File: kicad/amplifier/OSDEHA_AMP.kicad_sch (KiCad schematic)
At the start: 59 parts, among them J1 INPUT, J2 HEATERS DC, J3 PSU HV, J4 OUTPUT, J5 DHT FIL, Q1 DN2540, Q2 DN2540, Q3 STF3LN80K5, Q4 STF3LN80K5, SW1 SW_DPDT_x2, U1 6E5P, U2 6E5P, U3 801A, U4 801A

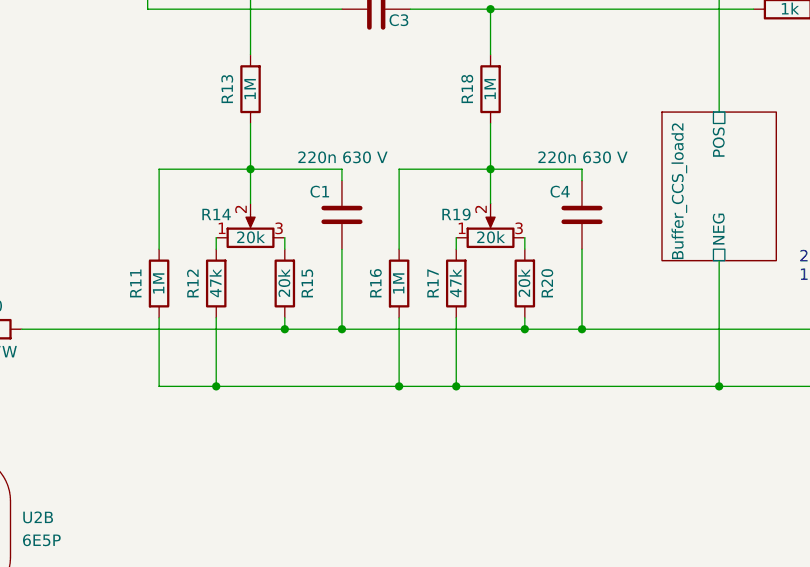
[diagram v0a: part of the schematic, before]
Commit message: adjust values of R15 and R20 by measurement of Vbias
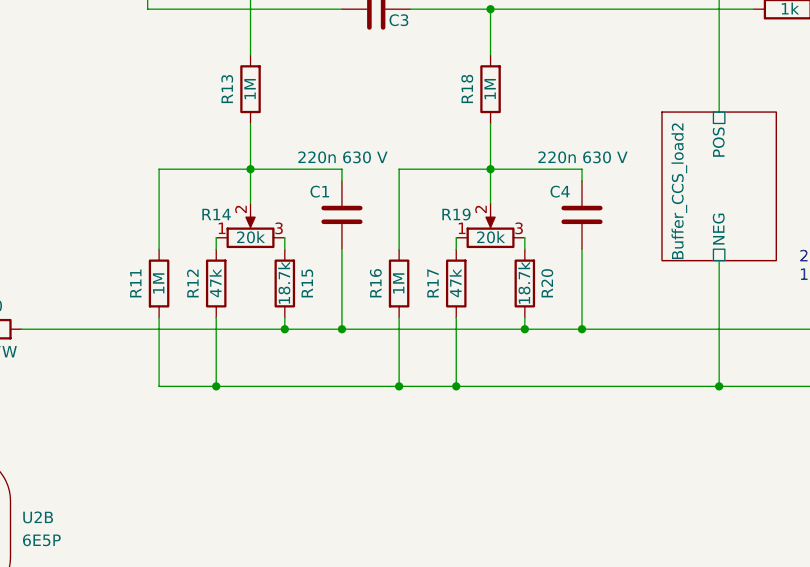
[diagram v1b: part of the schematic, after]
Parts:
- R15, R20: value 20k -> 18.7k
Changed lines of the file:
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@@
 			)
 		)
-		(property "Value" "20k"
+		(property "Value" "18.7k"
 			(at 191.77 173.99 90)
 			(effects
@@
 			)
 		)
-		(property "Value" "20k"
+		(property "Value" "18.7k"
 			(at 165.1 173.99 90)
 			(effects

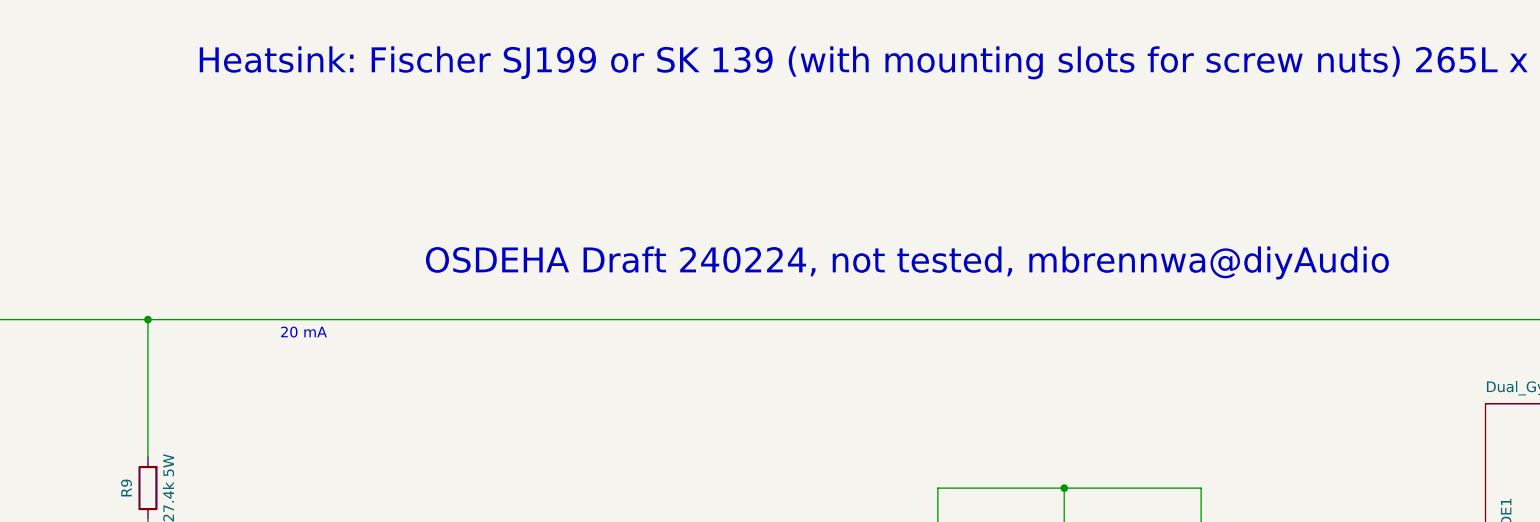
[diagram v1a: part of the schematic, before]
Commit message: draft date on schematic
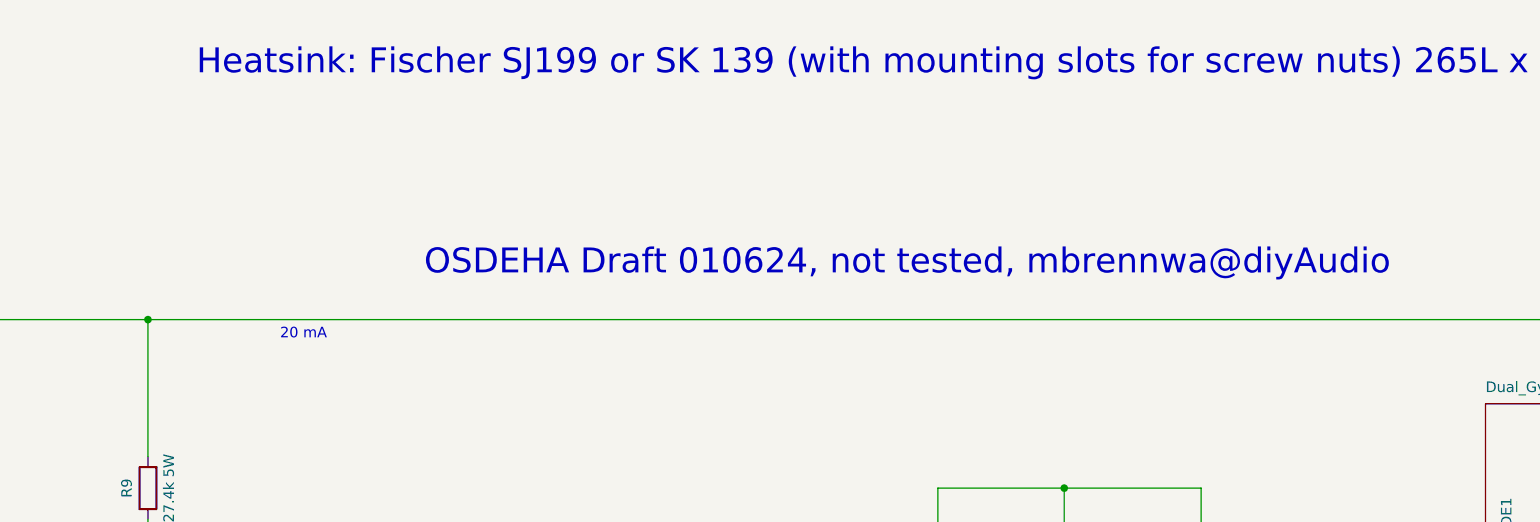
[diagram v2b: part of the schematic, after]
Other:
- note added: "OSDEHA Draft 010624, not tested, mbrennwa@diyAudio"
- note removed: "OSDEHA Draft 240224, not tested, mbrennwa@diyAudio"
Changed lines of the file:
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@@
 		)
 	)
-	(text "OSDEHA Draft 240224, not tested, mbrennwa@diyAudio"
+	(text "OSDEHA Draft 010624, not tested, mbrennwa@diyAudio"
 		(exclude_from_sim no)
 		(at 279.4 69.85 0)

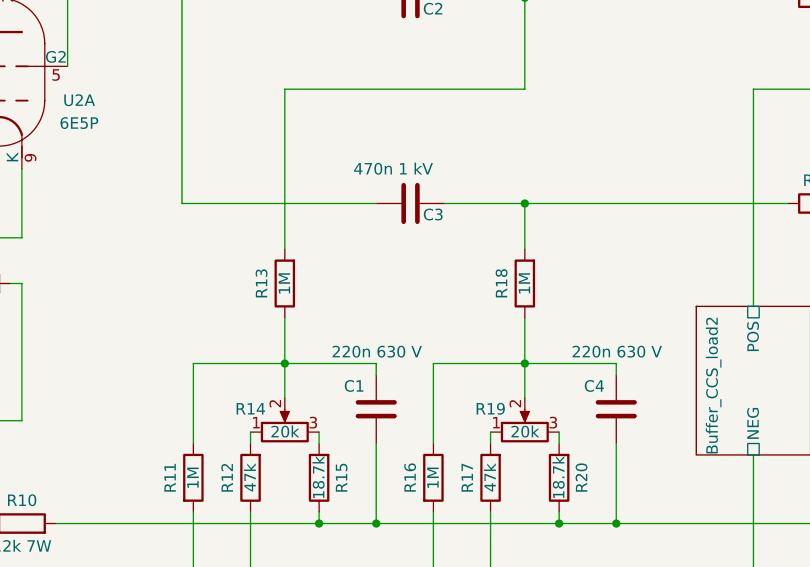
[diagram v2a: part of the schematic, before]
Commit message: changed R13 and R18 from 1M to 100k in schematic and PCB
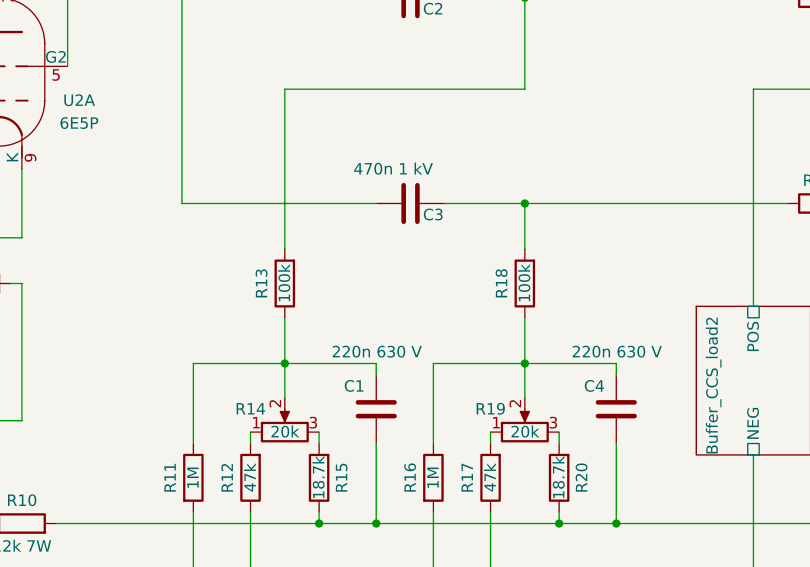
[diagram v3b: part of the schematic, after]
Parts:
- R13, R18: value 1M -> 100k
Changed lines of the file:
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@@
 			)
 		)
-		(property "Value" "1M"
+		(property "Value" "100k"
 			(at 161.29 152.4 90)
 			(effects
@@
 			)
 		)
-		(property "Value" "1M"
+		(property "Value" "100k"
 			(at 187.96 152.4 90)
 			(effects

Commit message: revise R values in schematic and PCB files. Expand test/design notes.
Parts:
- R13: MPN CMF551M0000 -> CMF55100K00
- R18: MPN CMF551M000 -> CMF55100K00
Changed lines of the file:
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@@
 			)
 		)
-		(property "MPN" "CMF551M0000"
+		(property "MPN" "CMF55100K00"
 			(at 161.29 152.4 90)
 			(effects
@@
 			)
 		)
-		(property "MPN" "CMF551M000"
+		(property "MPN" "CMF55100K00"
 			(at 187.96 152.4 90)
 			(effects

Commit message: cleanup
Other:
- note added: "OSDEHA Draft DDMMYY, not tested, mbrennwa@diyAudio"
- note removed: "OSDEHA Draft 010624, not tested, mbrennwa@diyAudio"
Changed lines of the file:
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@@
 		)
 	)
-	(text "OSDEHA Draft 010624, not tested, mbrennwa@diyAudio"
+	(text "OSDEHA Draft DDMMYY, not tested, mbrennwa@diyAudio"
 		(exclude_from_sim no)
 		(at 279.4 69.85 0)

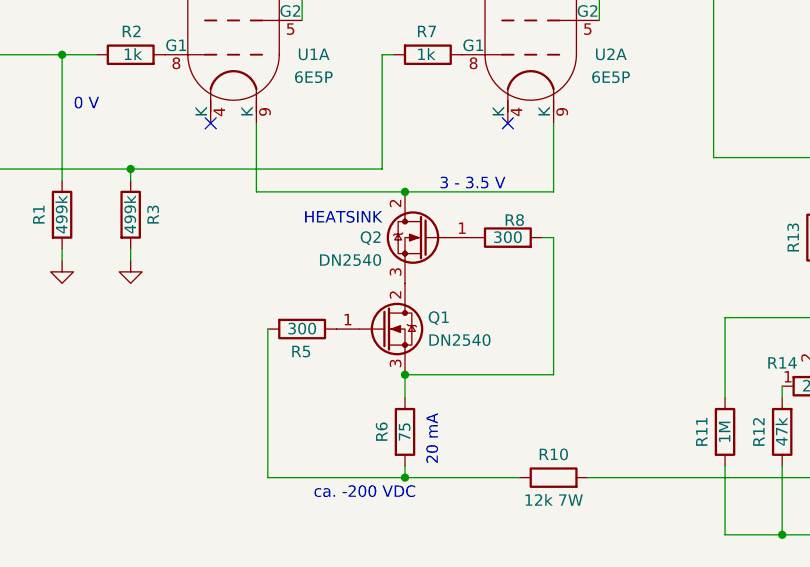
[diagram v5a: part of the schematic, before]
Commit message: gate stoppers 300R --> 1k
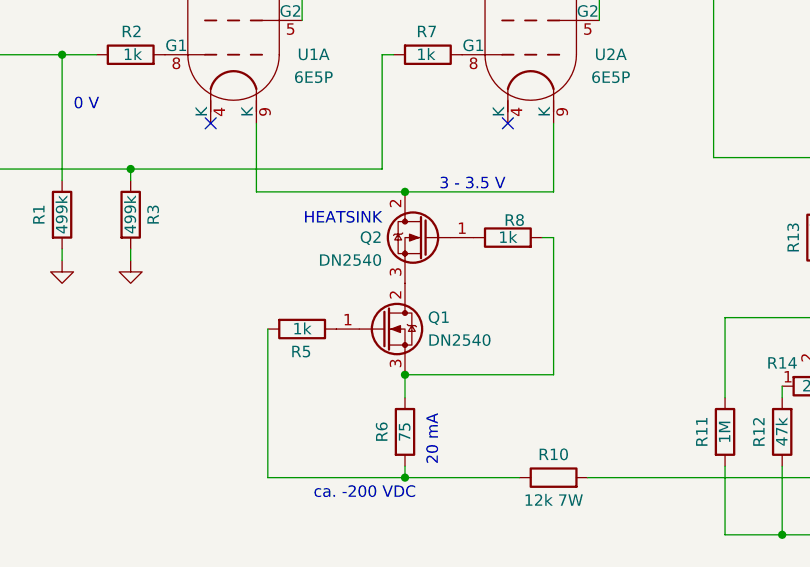
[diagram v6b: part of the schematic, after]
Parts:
- R5, R8: value 300 -> 1k; MPN CMF55300R00 -> CMF551K000
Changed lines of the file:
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@@
 		)
 		(stroke
-			(width 0)
+			(width 0.0254)
 			(type default)
 		)
@@
 			)
 		)
-		(property "Value" "300"
+		(property "Value" "1k"
 			(at 104.14 162.56 90)
 			(effects
@@
 			)
 		)
-		(property "MPN" "CMF55300R00"
+		(property "MPN" "CMF551K000"
 			(at 104.14 162.56 90)
 			(effects
@@
 			)
 		)
-		(property "Value" "300"
+		(property "Value" "1k"
 			(at 127 152.4 90)
 			(effects
@@
 			)
 		)
-		(property "MPN" "CMF55300R00"
+		(property "MPN" "CMF551K000"
 			(at 127 152.4 90)
 			(effects

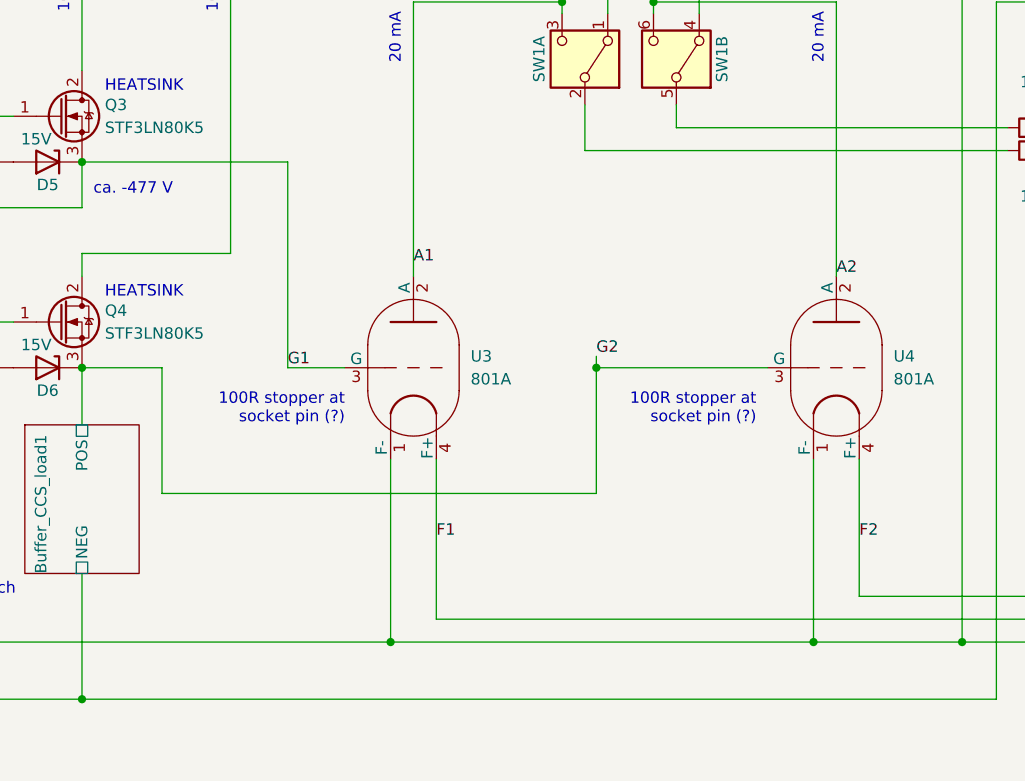
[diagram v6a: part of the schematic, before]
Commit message: add Zener clamp to DHT grids to prevent too much positive grid voltage
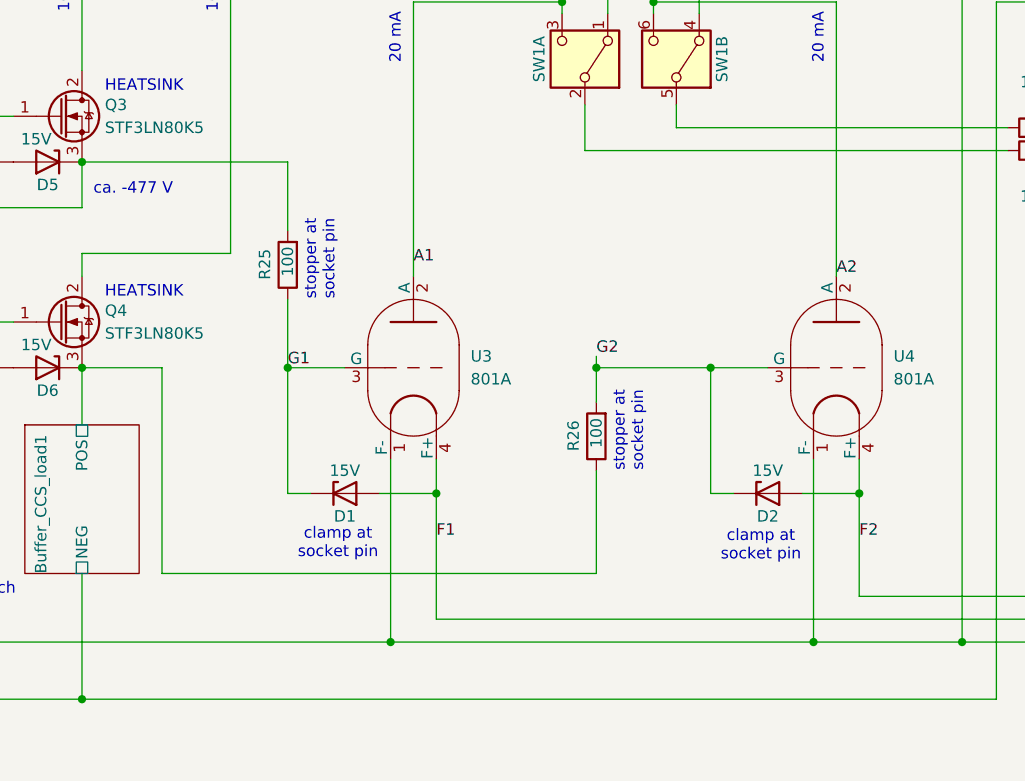
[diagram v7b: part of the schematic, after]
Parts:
- added D1, D2: 15V, Diode_THT:D_DO-41_SOD81_P7.62mm_Horizontal, symbol Device:D_Zener
- added R25, R26: 100, Resistor_THT:R_Axial_DIN0207_L6.3mm_D2.5mm_P10.16mm_Horizontal, symbol Device:R
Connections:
- net F1: now also D1.2 (A)
- net F2: now also D2.2 (A)
- net G1: now also D1.1 (K), R25.1; no longer D5.1 (K), Q3.3 (S)
- net G2: now also D2.1 (K), R26.2; no longer D6.1 (K), Q4.3 (S)
- new net Buffer_CCS_load1/POS: D6.1 (K), Q4.3 (S), R26.1
- new net Buffer_CCS_load2/POS: D5.1 (K), Q3.3 (S), R25.2
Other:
- note added: "clamp at socket pin"
- note added: "stopper at socket pin"
- note removed: "100R stopper at socket pin (?)"

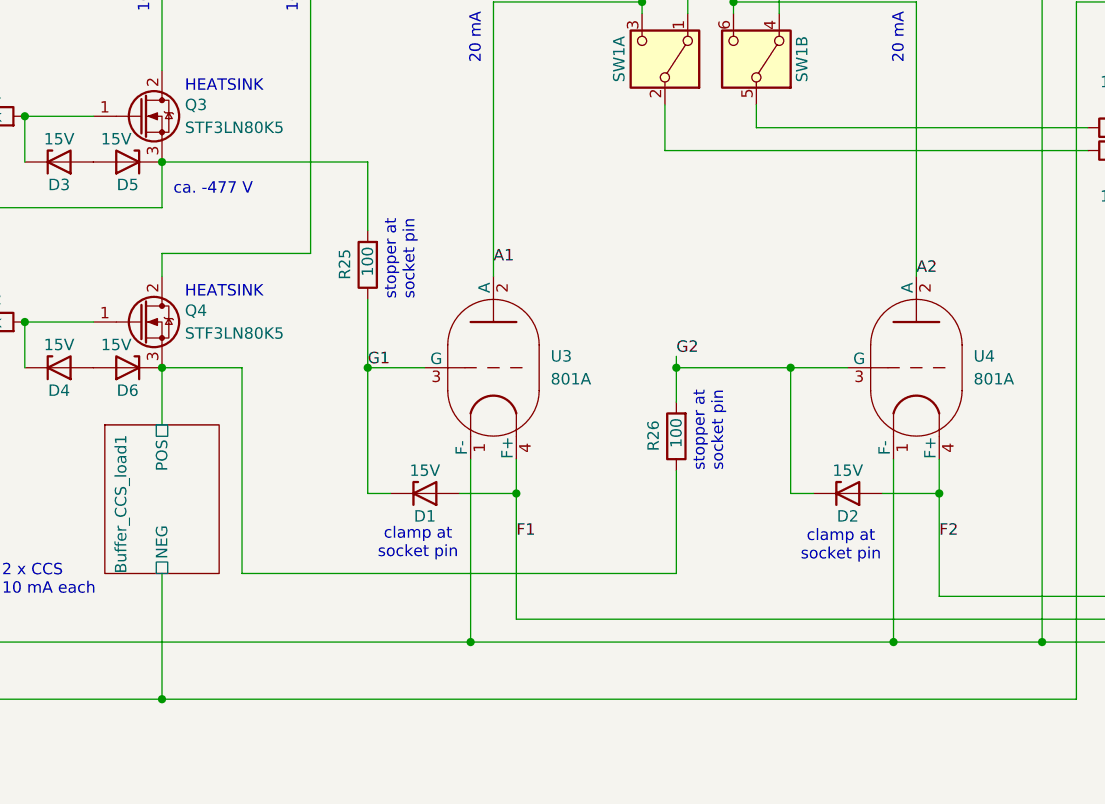
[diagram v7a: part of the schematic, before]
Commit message: revise diode clamp at DHT grids
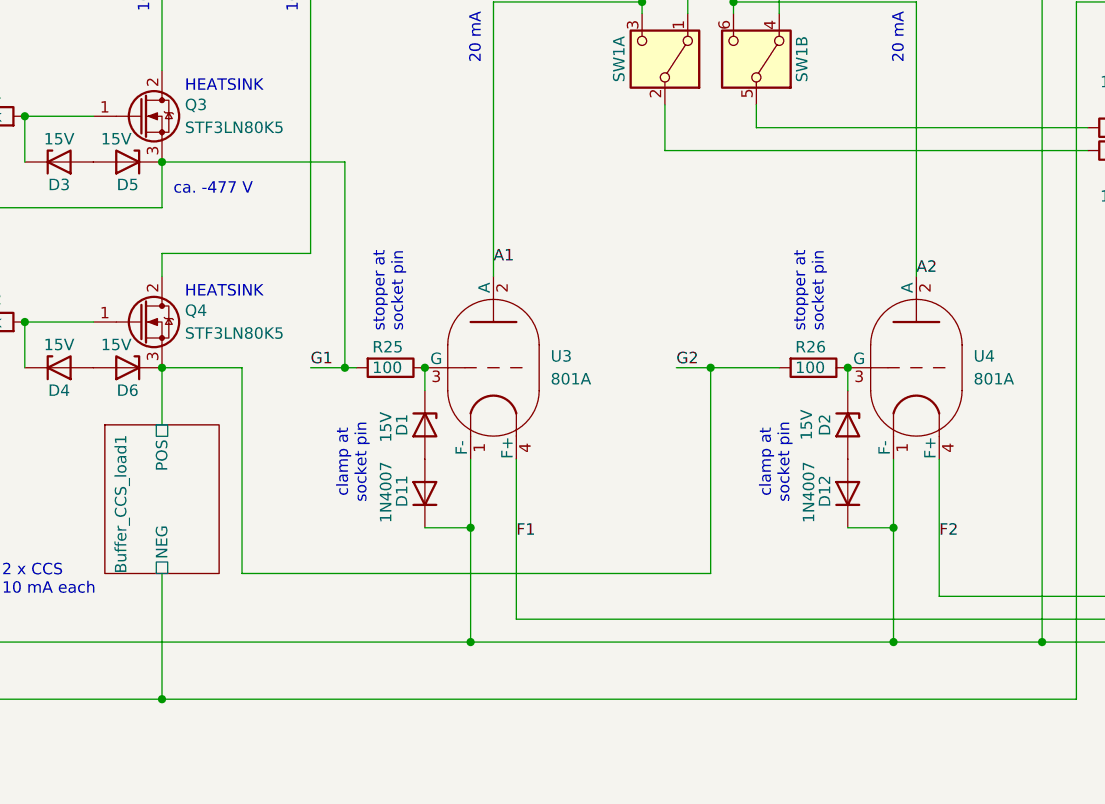
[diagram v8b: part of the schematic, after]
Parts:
- added D11, D12: 1N4007, Diode_THT:D_DO-41_SOD81_P10.16mm_Horizontal, symbol Diode:1N4007
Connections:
- net Buffer_CCS_load2/POS is gone; now on net G1: D5.1 (K), Q3.3 (S), R25.2
- net B-: now also D11.1 (K), D12.1 (K)
- net F1: no longer D1.2 (A)
- net F2: no longer D2.2 (A)
- net G1: no longer D1.1 (K), R25.1, U3.3 (G)
- net G2: now also D6.1 (K), Q4.3 (S); no longer D2.1 (K), U4.3 (G)
- removed net Buffer_CCS_load1/POS: D6.1 (K), Q4.3 (S), R26.1
- new net: D12.2 (A), D2.2 (A)
- new net: D1.2 (A), D11.2 (A)
- new net: D1.1 (K), R25.1, U3.3 (G)
- new net: D2.1 (K), R26.1, U4.3 (G)
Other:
- moved on the sheet: D1, D2, R25
